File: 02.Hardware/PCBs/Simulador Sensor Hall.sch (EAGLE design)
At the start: 23 parts

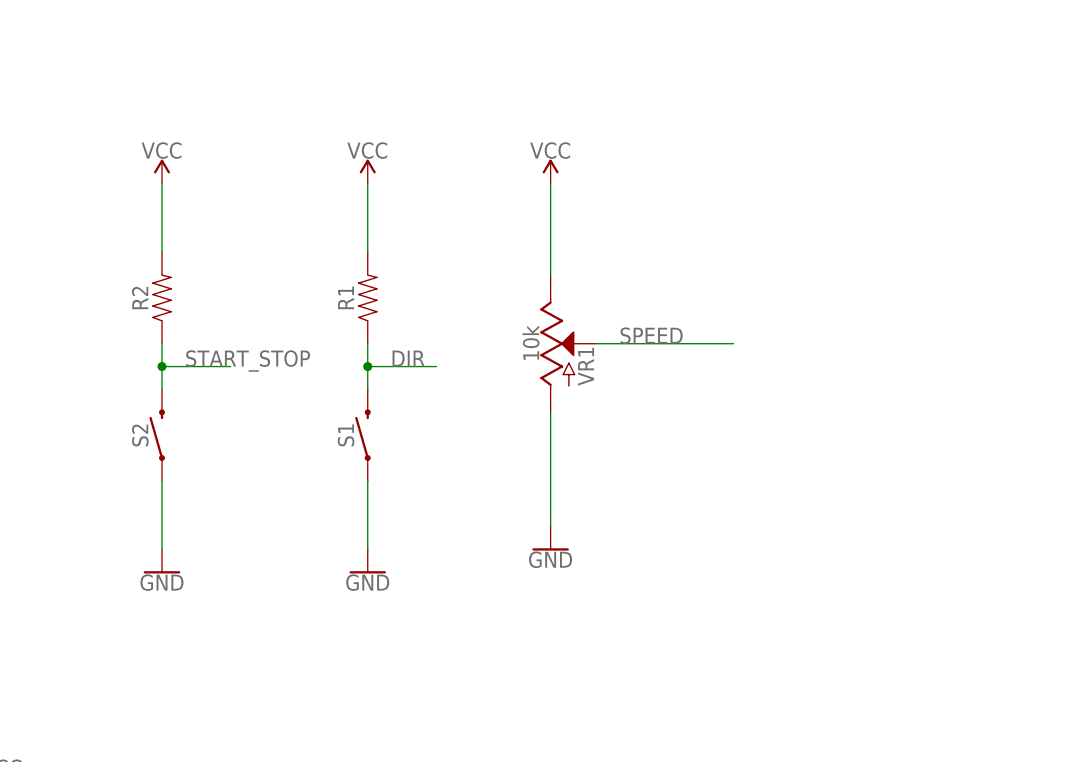
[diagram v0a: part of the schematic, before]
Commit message: Resistencias en serie en los pulsadores y potenciometro
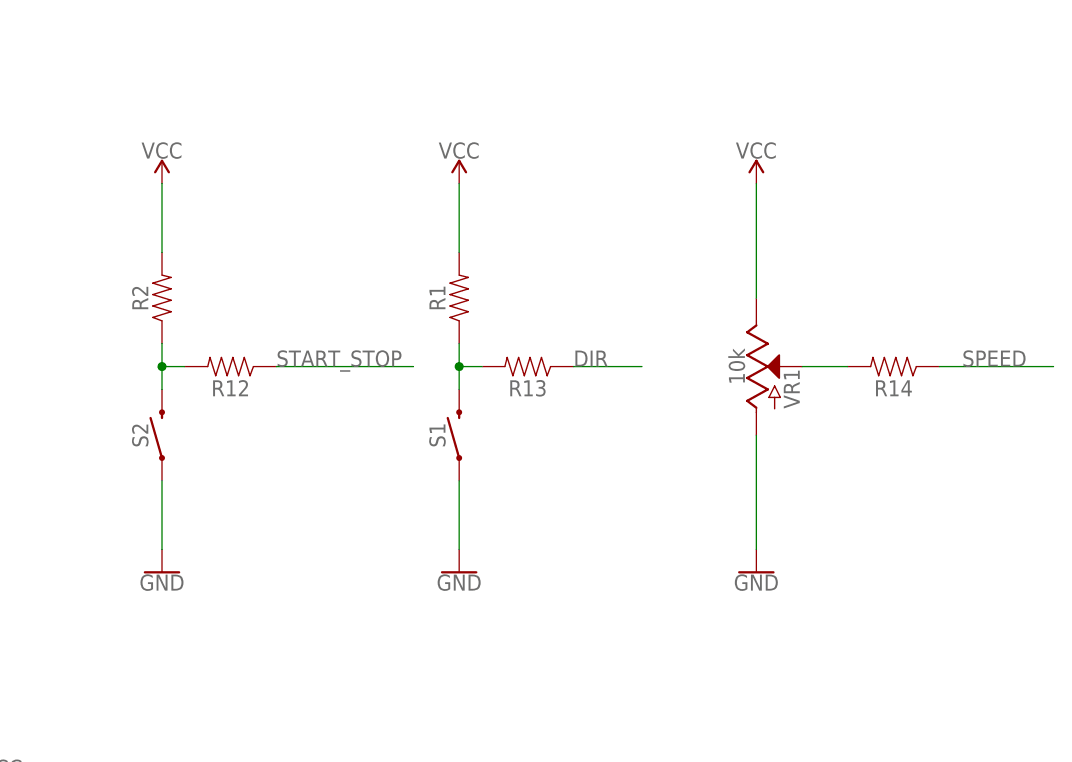
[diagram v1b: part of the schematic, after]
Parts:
- added R12, R13, R14: (no value), SparkFun-Resistors:RESISTOR0805
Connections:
- new net N$4: R12.2, R2.1, S2.2
- new net N$6: R1.1, R13.2, S1.2
- new net N$8: R14.2, VR1.S
- net DIR: now also R13.1; no longer R1.1, S1.2
- net SPEED: now also R14.1; no longer VR1.S
- net START_STOP: now also R12.1; no longer R2.1, S2.2
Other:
- moved on the sheet: R1, S1, VR1

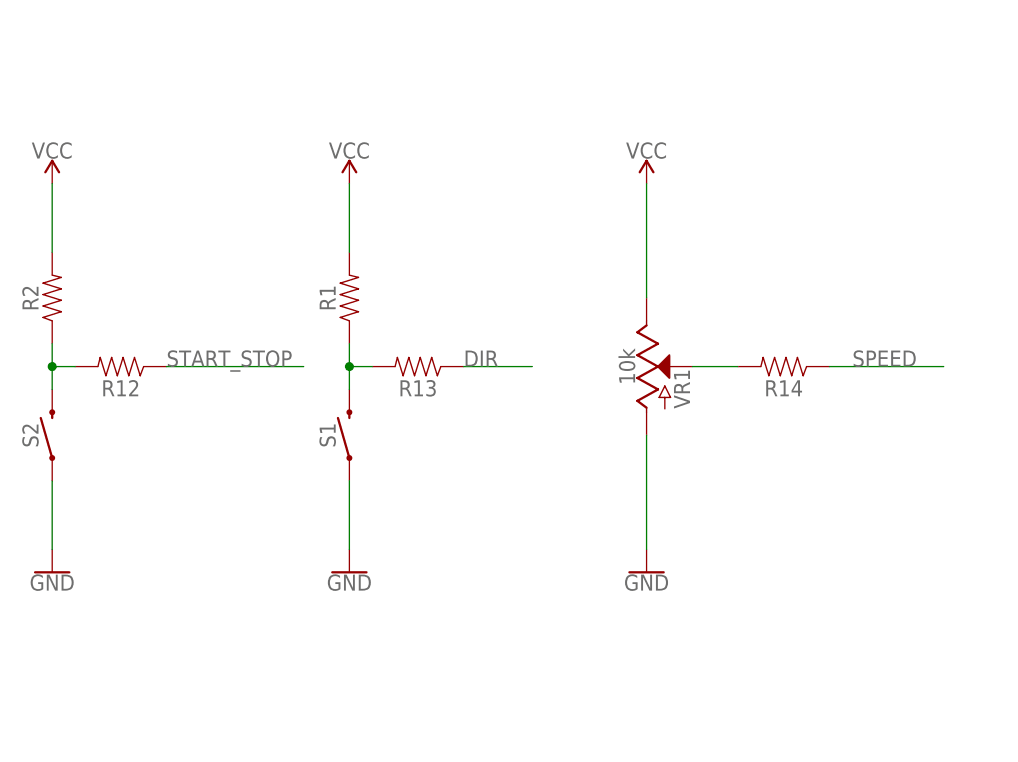
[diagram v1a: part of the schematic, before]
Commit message: Add RC Antirebotes
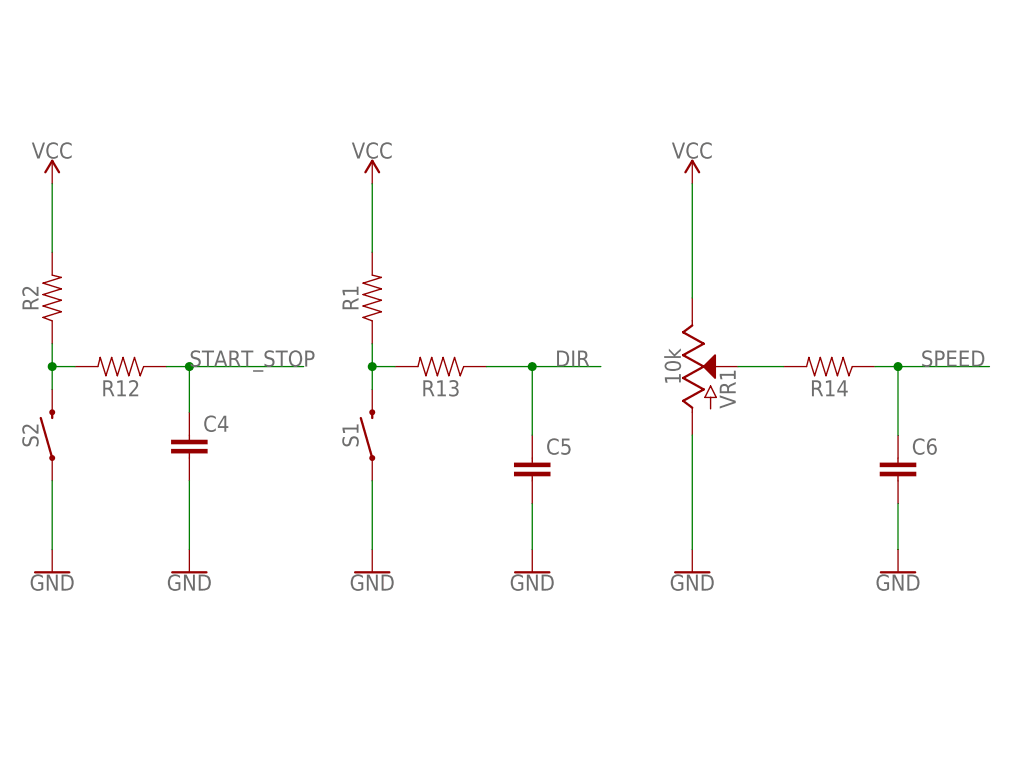
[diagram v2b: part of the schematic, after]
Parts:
- added C4, C5, C6: (no value), rcl:C-EUC0805K
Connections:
- net DIR: now also C5.1
- net GND: now also C4.2, C5.2, C6.2
- net SPEED: now also C6.1
- net START_STOP: now also C4.1
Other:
- moved on the sheet: R1, R13, R14, S1, VR1
